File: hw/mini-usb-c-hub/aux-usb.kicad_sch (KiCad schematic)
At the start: 2 parts, among them J301 USB_A

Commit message: chore(hw): lay-out some differential pairs
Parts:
- added C201: 10u, Capacitor_SMD:C_1206_3216Metric_Pad1.33x1.80mm_HandSolder, symbol Device:C
- renumbered D301 to D201, J301 to J201
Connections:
- net +5V: now also C201.1
- net GND: now also C201.2
- net USB+: now also D201.2 (I/O1); no longer D201.3 (I/O2)
- net USB-: now also D201.3 (I/O2); no longer D201.2 (I/O1)
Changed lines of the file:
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@@
 	(paper "A4")
 	(junction
-		(at 118.11 88.9)
+		(at 156.21 97.79)
 		(diameter 0)
 		(color 0 0 0 0)
 	)
 	(junction
-		(at 143.51 86.36)
+		(at 144.78 69.85)
+		(diameter 0)
+		(color 0 0 0 0)
+	)
+	(junction
+		(at 118.11 86.36)
 		(diameter 0)
 		(color 0 0 0 0)
@@
 		(color 0 0 0 0)
 	)
-	(wire
-		(pts
-			(xy 143.51 86.36) (xy 143.51 102.87)
-		)
-		(stroke
-			(width 0)
-			(type default)
-		)
+	(junction
+		(at 143.51 88.9)
+		(diameter 0)
+		(color 0 0 0 0)
 	)
 	(wire
@@
 	(wire
 		(pts
+			(xy 163.83 97.79) (xy 156.21 97.79)
+		)
+		(stroke
+			(width 0)
+			(type default)
+		)
+	)
+	(wire
+		(pts
+			(xy 143.51 88.9) (xy 146.05 88.9)
+		)
+		(stroke
+			(width 0)
+			(type default)
+		)
+	)
+	(wire
+		(pts
 			(xy 153.67 96.52) (xy 153.67 97.79)
 		)
@@
 	(wire
 		(pts
-			(xy 118.11 88.9) (xy 118.11 102.87)
-		)
-		(stroke
-			(width 0)
-			(type default)
-		)
-	)
-	(wire
-		(pts
-			(xy 143.51 80.01) (xy 143.51 81.28)
-		)
-		(stroke
-			(width 0)
-			(type default)
-		)
-	)
-	(wire
-		(pts
-			(xy 143.51 86.36) (xy 109.22 86.36)
-		)
-		(stroke
-			(width 0)
-			(type default)
-		)
-	)
-	(wire
-		(pts
-			(xy 143.51 81.28) (xy 146.05 81.28)
-		)
-		(stroke
-			(width 0)
-			(type default)
-		)
-	)
-	(wire
-		(pts
-			(xy 118.11 88.9) (xy 109.22 88.9)
-		)
-		(stroke
-			(width 0)
-			(type default)
-		)
-	)
-	(wire
-		(pts
-			(xy 146.05 86.36) (xy 143.51 86.36)
-		)
-		(stroke
-			(width 0)
-			(type default)
-		)
-	)
-	(wire
-		(pts
-			(xy 146.05 88.9) (xy 118.11 88.9)
+			(xy 118.11 86.36) (xy 118.11 102.87)
+		)
+		(stroke
+			(width 0)
+			(type default)
+		)
+	)
+	(wire
+		(pts
+			(xy 144.78 67.31) (xy 144.78 69.85)
+		)
+		(stroke
+			(width 0)
+			(type default)
+		)
+	)
+	(wire
+		(pts
+			(xy 163.83 82.55) (xy 163.83 69.85)
+		)
+		(stroke
+			(width 0)
+			(type default)
+		)
+	)
+	(wire
+		(pts
+			(xy 109.22 86.36) (xy 118.11 86.36)
+		)
+		(stroke
+			(width 0)
+			(type default)
+		)
+	)
+	(wire
+		(pts
+			(xy 163.83 69.85) (xy 144.78 69.85)
+		)
+		(stroke
+			(width 0)
+			(type default)
+		)
+	)
+	(wire
+		(pts
+			(xy 144.78 81.28) (xy 146.05 81.28)
+		)
+		(stroke
+			(width 0)
+			(type default)
+		)
+	)
+	(wire
+		(pts
+			(xy 144.78 69.85) (xy 144.78 81.28)
+		)
+		(stroke
+			(width 0)
+			(type default)
+		)
+	)
+	(wire
+		(pts
+			(xy 143.51 88.9) (xy 143.51 102.87)
+		)
+		(stroke
+			(width 0)
+			(type default)
+		)
+	)
+	(wire
+		(pts
+			(xy 163.83 90.17) (xy 163.83 97.79)
+		)
+		(stroke
+			(width 0)
+			(type default)
+		)
+	)
+	(wire
+		(pts
+			(xy 118.11 86.36) (xy 146.05 86.36)
+		)
+		(stroke
+			(width 0)
+			(type default)
+		)
+	)
+	(wire
+		(pts
+			(xy 109.22 88.9) (xy 143.51 88.9)
 		)
 		(stroke
@@
 			)
 			(justify right)
+		)
+	)
+	(symbol
+		(lib_id "Device:C")
+		(at 163.83 86.36 0)
+		(unit 1)
+		(exclude_from_sim no)
+		(in_bom yes)
+		(on_board yes)
+		(dnp no)
+		(fields_autoplaced yes)
+		(property "Reference" "C201"
+			(at 167.64 85.0899 0)
+			(effects
+				(font
+					(size 1.27 1.27)
+				)
+				(justify left)
+			)
+		)
+		(property "Value" "10u"
+			(at 167.64 87.6299 0)
+			(effects
+				(font
+					(size 1.27 1.27)
+				)
+				(justify left)
+			)
+		)
+		(property "Footprint" "Capacitor_SMD:C_1206_3216Metric_Pad1.33x1.80mm_HandSolder"
+			(at 164.7952 90.17 0)
+			(effects
+				(font
+					(size 1.27 1.27)
+				)
+				(hide yes)
+			)
+		)
+		(property "Datasheet" "~"
+			(at 163.83 86.36 0)
+			(effects
+				(font
+					(size 1.27 1.27)
+				)
+				(hide yes)
+			)
+		)
+		(property "Description" "Unpolarized capacitor"
+			(at 163.83 86.36 0)
+			(effects
+				(font
+					(size 1.27 1.27)
+				)
+				(hide yes)
+			)
+		)
+		(pin "2"
+		)
+		(pin "1"
+		)
+		(instances
+			(project ""
+				(path "/7c04e056-0d84-4da3-ae50-c0eef25c6fa4/3a3338ad-7d0d-429a-9ebe-8c6db2f36fb7"
+					(reference "C201")
+					(unit 1)
+				)
+				(path "/7c04e056-0d84-4da3-ae50-c0eef25c6fa4/6954961b-de3c-4bca-aa61-d117dae2b824"
+					(reference "C301")
+					(unit 1)
+				)
+				(path "/7c04e056-0d84-4da3-ae50-c0eef25c6fa4/d5fb26e1-6ffb-4d31-86a3-773e4f702a40"
+					(reference "C401")
+					(unit 1)
+				)
+			)
 		)
 	)
@@
 		(dnp no)
 		(fields_autoplaced yes)
-		(property "Reference" "#PWR0301"
+		(property "Reference" "#PWR0202"
 			(at 130.81 88.9 0)
 			(effects
@@
 			(project "mini-usb-c-hub"
 				(path "/7c04e056-0d84-4da3-ae50-c0eef25c6fa4/3a3338ad-7d0d-429a-9ebe-8c6db2f36fb7"
-					(reference "#PWR0301")
+					(reference "#PWR0202")
 					(unit 1)
 				)
 				(path "/7c04e056-0d84-4da3-ae50-c0eef25c6fa4/6954961b-de3c-4bca-aa61-d117dae2b824"
-					(reference "#PWR0401")
+					(reference "#PWR0302")
 					(unit 1)
 				)
 				(path "/7c04e056-0d84-4da3-ae50-c0eef25c6fa4/d5fb26e1-6ffb-4d31-86a3-773e4f702a40"
-					(reference "#PWR0501")
+					(reference "#PWR0402")
 					(unit 1)
 				)
@@
 		(dnp no)
 		(fields_autoplaced yes)
-		(property "Reference" "#PWR0302"
+		(property "Reference" "#PWR0204"
 			(at 130.81 121.92 0)
 			(effects
@@
 			(project "mini-usb-c-hub"
 				(path "/7c04e056-0d84-4da3-ae50-c0eef25c6fa4/3a3338ad-7d0d-429a-9ebe-8c6db2f36fb7"
-					(reference "#PWR0302")
+					(reference "#PWR0204")
 					(unit 1)
 				)
 				(path "/7c04e056-0d84-4da3-ae50-c0eef25c6fa4/6954961b-de3c-4bca-aa61-d117dae2b824"
-					(reference "#PWR0402")
+					(reference "#PWR0304")
 					(unit 1)
 				)
 				(path "/7c04e056-0d84-4da3-ae50-c0eef25c6fa4/d5fb26e1-6ffb-4d31-86a3-773e4f702a40"
-					(reference "#PWR0502")
+					(reference "#PWR0404")
 					(unit 1)
 				)
@@
 		(on_board yes)
 		(dnp no)
-		(property "Reference" "D301"
+		(property "Reference" "D201"
 			(at 142.24 110.49 0)
 			(effects
@@
 			(project "mini-usb-c-hub"
 				(path "/7c04e056-0d84-4da3-ae50-c0eef25c6fa4/3a3338ad-7d0d-429a-9ebe-8c6db2f36fb7"
+					(reference "D201")
+					(unit 1)
+				)
+				(path "/7c04e056-0d84-4da3-ae50-c0eef25c6fa4/6954961b-de3c-4bca-aa61-d117dae2b824"
 					(reference "D301")
 					(unit 1)
 				)
-				(path "/7c04e056-0d84-4da3-ae50-c0eef25c6fa4/6954961b-de3c-4bca-aa61-d117dae2b824"
+				(path "/7c04e056-0d84-4da3-ae50-c0eef25c6fa4/d5fb26e1-6ffb-4d31-86a3-773e4f702a40"
 					(reference "D401")
-					(unit 1)
-				)
-				(path "/7c04e056-0d84-4da3-ae50-c0eef25c6fa4/d5fb26e1-6ffb-4d31-86a3-773e4f702a40"
-					(reference "D501")
 					(unit 1)
 				)
@@
 		(dnp no)
 		(fields_autoplaced yes)
-		(property "Reference" "J301"
+		(property "Reference" "J201"
 			(at 153.67 73.66 0)
 			(effects
@@
 			(project "mini-usb-c-hub"
 				(path "/7c04e056-0d84-4da3-ae50-c0eef25c6fa4/3a3338ad-7d0d-429a-9ebe-8c6db2f36fb7"
+					(reference "J201")
+					(unit 1)
+				)
+				(path "/7c04e056-0d84-4da3-ae50-c0eef25c6fa4/6954961b-de3c-4bca-aa61-d117dae2b824"
 					(reference "J301")
 					(unit 1)
 				)
-				(path "/7c04e056-0d84-4da3-ae50-c0eef25c6fa4/6954961b-de3c-4bca-aa61-d117dae2b824"
+				(path "/7c04e056-0d84-4da3-ae50-c0eef25c6fa4/d5fb26e1-6ffb-4d31-86a3-773e4f702a40"
 					(reference "J401")
-					(unit 1)
-				)
-				(path "/7c04e056-0d84-4da3-ae50-c0eef25c6fa4/d5fb26e1-6ffb-4d31-86a3-773e4f702a40"
-					(reference "J501")
 					(unit 1)
 				)
@@
 	(symbol
 		(lib_id "power:+5V")
-		(at 143.51 80.01 0)
+		(at 144.78 67.31 0)
 		(unit 1)
 		(exclude_from_sim no)
@@
 		(dnp no)
 		(fields_autoplaced yes)
-		(property "Reference" "#PWR0303"
-			(at 143.51 83.82 0)
+		(property "Reference" "#PWR0201"
+			(at 144.78 71.12 0)
 			(effects
 				(font
@@
 		)
 		(property "Value" "+5V"
-			(at 143.51 74.93 0)
+			(at 144.78 62.23 0)
 			(effects
 				(font
@@
 		)
 		(property "Footprint" ""
-			(at 143.51 80.01 0)
+			(at 144.78 67.31 0)
 			(effects
 				(font
@@
 		)
 		(property "Datasheet" ""
-			(at 143.51 80.01 0)
+			(at 144.78 67.31 0)
 			(effects
 				(font
@@
 		)
 		(property "Description" "Power symbol creates a global label with name \"+5V\""
-			(at 143.51 80.01 0)
+			(at 144.78 67.31 0)
 			(effects
 				(font
@@
 			(project "mini-usb-c-hub"
 				(path "/7c04e056-0d84-4da3-ae50-c0eef25c6fa4/3a3338ad-7d0d-429a-9ebe-8c6db2f36fb7"
-					(reference "#PWR0303")
+					(reference "#PWR0201")
 					(unit 1)
 				)
 				(path "/7c04e056-0d84-4da3-ae50-c0eef25c6fa4/6954961b-de3c-4bca-aa61-d117dae2b824"
-					(reference "#PWR0403")
+					(reference "#PWR0301")
 					(unit 1)
 				)
 				(path "/7c04e056-0d84-4da3-ae50-c0eef25c6fa4/d5fb26e1-6ffb-4d31-86a3-773e4f702a40"
-					(reference "#PWR0503")
+					(reference "#PWR0401")
 					(unit 1)
 				)
@@
 		(dnp no)
 		(fields_autoplaced yes)
-		(property "Reference" "#PWR0304"
+		(property "Reference" "#PWR0203"
 			(at 153.67 106.68 0)
 			(effects
@@
 			(project "mini-usb-c-hub"
 				(path "/7c04e056-0d84-4da3-ae50-c0eef25c6fa4/3a3338ad-7d0d-429a-9ebe-8c6db2f36fb7"
-					(reference "#PWR0304")
+					(reference "#PWR0203")
 					(unit 1)
 				)
 				(path "/7c04e056-0d84-4da3-ae50-c0eef25c6fa4/6954961b-de3c-4bca-aa61-d117dae2b824"
-					(reference "#PWR0404")
+					(reference "#PWR0303")
 					(unit 1)
 				)
 				(path "/7c04e056-0d84-4da3-ae50-c0eef25c6fa4/d5fb26e1-6ffb-4d31-86a3-773e4f702a40"
-					(reference "#PWR0504")
-					(unit 1)
-				)
+					(reference "#PWR0403")
+					(unit 1)
+				)

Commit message: chore(hw): update layout, fix references
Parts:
- renumbered C201 to C501, D201 to D501, J201 to J501
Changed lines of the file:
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@@
 		(dnp no)
 		(fields_autoplaced yes)
-		(property "Reference" "C201"
+		(property "Reference" "C501"
 			(at 167.64 85.0899 0)
 			(effects
@@
 			(project ""
 				(path "/7c04e056-0d84-4da3-ae50-c0eef25c6fa4/3a3338ad-7d0d-429a-9ebe-8c6db2f36fb7"
-					(reference "C201")
-					(unit 1)
-				)
-				(path "/7c04e056-0d84-4da3-ae50-c0eef25c6fa4/6954961b-de3c-4bca-aa61-d117dae2b824"
-					(reference "C301")
+					(reference "C501")
+					(unit 1)
+				)
+				(path "/7c04e056-0d84-4da3-ae50-c0eef25c6fa4/6954961b-de3c-4bca-aa61-d117dae2b824"
+					(reference "C401")
 					(unit 1)
 				)
@@
 		(dnp no)
 		(fields_autoplaced yes)
-		(property "Reference" "#PWR0202"
+		(property "Reference" "#PWR0501"
 			(at 130.81 88.9 0)
 			(effects
@@
 			(project "mini-usb-c-hub"
 				(path "/7c04e056-0d84-4da3-ae50-c0eef25c6fa4/3a3338ad-7d0d-429a-9ebe-8c6db2f36fb7"
-					(reference "#PWR0202")
-					(unit 1)
-				)
-				(path "/7c04e056-0d84-4da3-ae50-c0eef25c6fa4/6954961b-de3c-4bca-aa61-d117dae2b824"
-					(reference "#PWR0302")
+					(reference "#PWR0501")
+					(unit 1)
+				)
+				(path "/7c04e056-0d84-4da3-ae50-c0eef25c6fa4/6954961b-de3c-4bca-aa61-d117dae2b824"
+					(reference "#PWR0401")
 					(unit 1)
 				)
@@
 		(dnp no)
 		(fields_autoplaced yes)
-		(property "Reference" "#PWR0204"
+		(property "Reference" "#PWR0502"
 			(at 130.81 121.92 0)
 			(effects
@@
 			(project "mini-usb-c-hub"
 				(path "/7c04e056-0d84-4da3-ae50-c0eef25c6fa4/3a3338ad-7d0d-429a-9ebe-8c6db2f36fb7"
-					(reference "#PWR0204")
-					(unit 1)
-				)
-				(path "/7c04e056-0d84-4da3-ae50-c0eef25c6fa4/6954961b-de3c-4bca-aa61-d117dae2b824"
-					(reference "#PWR0304")
+					(reference "#PWR0502")
+					(unit 1)
+				)
+				(path "/7c04e056-0d84-4da3-ae50-c0eef25c6fa4/6954961b-de3c-4bca-aa61-d117dae2b824"
+					(reference "#PWR0402")
 					(unit 1)
 				)
@@
 		(on_board yes)
 		(dnp no)
-		(property "Reference" "D201"
+		(property "Reference" "D501"
 			(at 142.24 110.49 0)
 			(effects
@@
 			(project "mini-usb-c-hub"
 				(path "/7c04e056-0d84-4da3-ae50-c0eef25c6fa4/3a3338ad-7d0d-429a-9ebe-8c6db2f36fb7"
-					(reference "D201")
-					(unit 1)
-				)
-				(path "/7c04e056-0d84-4da3-ae50-c0eef25c6fa4/6954961b-de3c-4bca-aa61-d117dae2b824"
-					(reference "D301")
+					(reference "D501")
+					(unit 1)
+				)
+				(path "/7c04e056-0d84-4da3-ae50-c0eef25c6fa4/6954961b-de3c-4bca-aa61-d117dae2b824"
+					(reference "D401")
 					(unit 1)
 				)
@@
 		(dnp no)
 		(fields_autoplaced yes)
-		(property "Reference" "J201"
+		(property "Reference" "J501"
 			(at 153.67 73.66 0)
 			(effects
@@
 			(project "mini-usb-c-hub"
 				(path "/7c04e056-0d84-4da3-ae50-c0eef25c6fa4/3a3338ad-7d0d-429a-9ebe-8c6db2f36fb7"
-					(reference "J201")
-					(unit 1)
-				)
-				(path "/7c04e056-0d84-4da3-ae50-c0eef25c6fa4/6954961b-de3c-4bca-aa61-d117dae2b824"
-					(reference "J301")
+					(reference "J501")
+					(unit 1)
+				)
+				(path "/7c04e056-0d84-4da3-ae50-c0eef25c6fa4/6954961b-de3c-4bca-aa61-d117dae2b824"
+					(reference "J401")
 					(unit 1)
 				)
@@
 		(dnp no)
 		(fields_autoplaced yes)
-		(property "Reference" "#PWR0201"
+		(property "Reference" "#PWR0503"
 			(at 144.78 71.12 0)
 			(effects
@@
 			(project "mini-usb-c-hub"
 				(path "/7c04e056-0d84-4da3-ae50-c0eef25c6fa4/3a3338ad-7d0d-429a-9ebe-8c6db2f36fb7"
-					(reference "#PWR0201")
-					(unit 1)
-				)
-				(path "/7c04e056-0d84-4da3-ae50-c0eef25c6fa4/6954961b-de3c-4bca-aa61-d117dae2b824"
-					(reference "#PWR0301")
+					(reference "#PWR0503")
+					(unit 1)
+				)
+				(path "/7c04e056-0d84-4da3-ae50-c0eef25c6fa4/6954961b-de3c-4bca-aa61-d117dae2b824"
+					(reference "#PWR0403")
 					(unit 1)
 				)
@@
 		(dnp no)
 		(fields_autoplaced yes)
-		(property "Reference" "#PWR0203"
+		(property "Reference" "#PWR0504"
 			(at 153.67 106.68 0)
 			(effects
@@
 			(project "mini-usb-c-hub"
 				(path "/7c04e056-0d84-4da3-ae50-c0eef25c6fa4/3a3338ad-7d0d-429a-9ebe-8c6db2f36fb7"
-					(reference "#PWR0203")
-					(unit 1)
-				)
-				(path "/7c04e056-0d84-4da3-ae50-c0eef25c6fa4/6954961b-de3c-4bca-aa61-d117dae2b824"
-					(reference "#PWR0303")
-					(unit 1)
-				)
+					(reference "#PWR0504")
+					(unit 1)
+				)
+				(path "/7c04e056-0d84-4da3-ae50-c0eef25c6fa4/6954961b-de3c-4bca-aa61-d117dae2b824"
+					(reference "#PWR0404")
+					(unit 1)
+				)

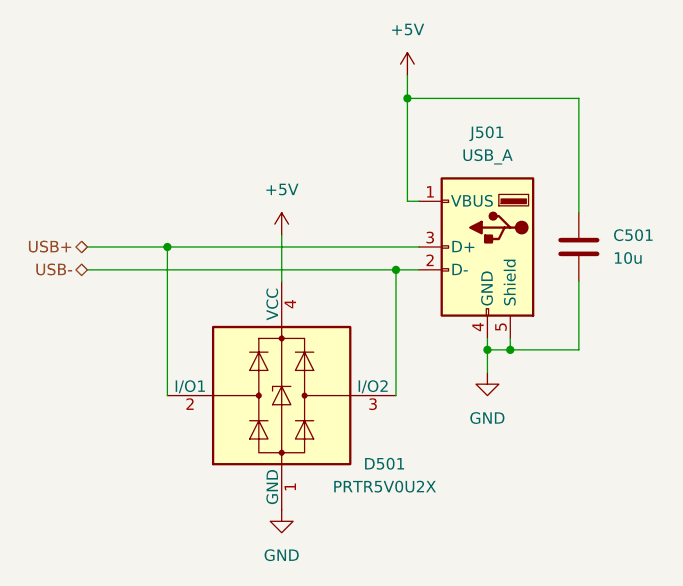
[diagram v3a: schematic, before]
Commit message: chore(hw): switch to KiCad 9.0
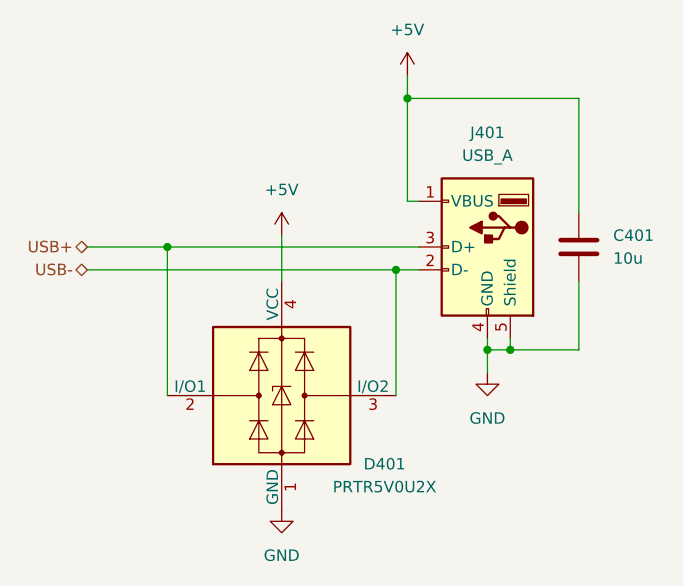
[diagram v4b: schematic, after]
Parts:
- renumbered C501 to C401, D501 to D401, J501 to J401
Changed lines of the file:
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@@
 (kicad_sch
-	(version 20231120)
+	(version 20250114)
 	(generator "eeschema")
-	(generator_version "8.0")
+	(generator_version "9.0")
 	(paper "A4")
 	(junction
@@
 		(shape bidirectional)
 		(at 109.22 86.36 180)
-		(fields_autoplaced yes)
 		(effects
 			(font
@@
 		(shape bidirectional)
 		(at 109.22 88.9 180)
-		(fields_autoplaced yes)
 		(effects
 			(font
@@
 		(dnp no)
 		(fields_autoplaced yes)
-		(property "Reference" "C501"
+		(property "Reference" "C401"
 			(at 167.64 85.0899 0)
 			(effects
@@
 		(dnp no)
 		(fields_autoplaced yes)
-		(property "Reference" "#PWR0501"
+		(property "Reference" "#PWR0401"
 			(at 130.81 88.9 0)
 			(effects
@@
 		(dnp no)
 		(fields_autoplaced yes)
-		(property "Reference" "#PWR0502"
+		(property "Reference" "#PWR0402"
 			(at 130.81 121.92 0)
 			(effects
@@
 		(on_board yes)
 		(dnp no)
-		(property "Reference" "D501"
+		(property "Reference" "D401"
 			(at 142.24 110.49 0)
 			(effects
@@
 		(dnp no)
 		(fields_autoplaced yes)
-		(property "Reference" "J501"
+		(property "Reference" "J401"
 			(at 153.67 73.66 0)
 			(effects
@@
 		(dnp no)
 		(fields_autoplaced yes)
-		(property "Reference" "#PWR0503"
+		(property "Reference" "#PWR0403"
 			(at 144.78 71.12 0)
 			(effects
@@
 		(dnp no)
 		(fields_autoplaced yes)
-		(property "Reference" "#PWR0504"
+		(property "Reference" "#PWR0404"
 			(at 153.67 106.68 0)
 			(effects
